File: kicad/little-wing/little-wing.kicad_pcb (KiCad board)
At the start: 4 copper layers, 16.1 x 57.1 mm, 45 parts, among them J1 HRO_TYPE-C-31-M-14, J2 Battery, J3 rgb, J4 columns, J5 Conn_01x10, J6 rows, J7 sensor, SW1 Battery, SW2 Reset, U1 nRF52840_CKAA, U2 nPM1100-CAAx, X1 32MHz, X2 32.768kHz

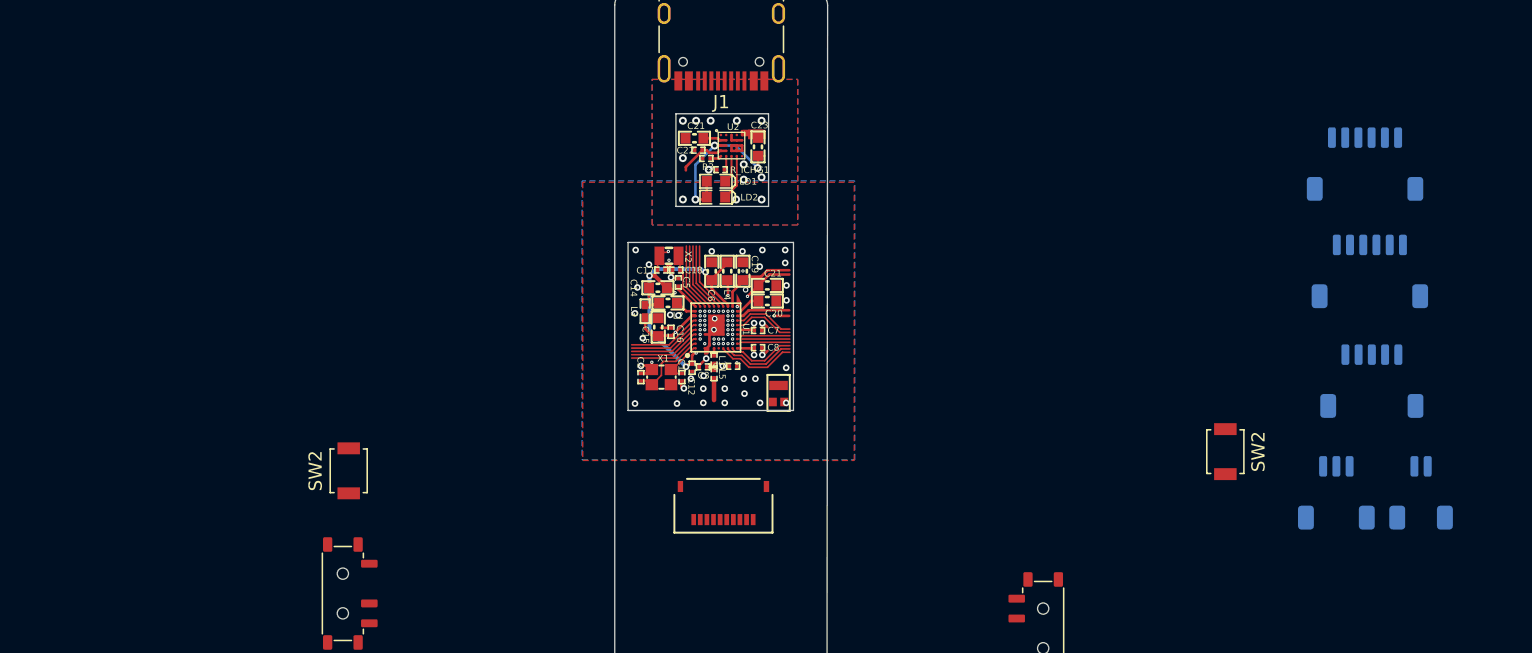
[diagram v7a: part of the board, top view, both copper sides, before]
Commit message: Cleaning up some space on the PCB
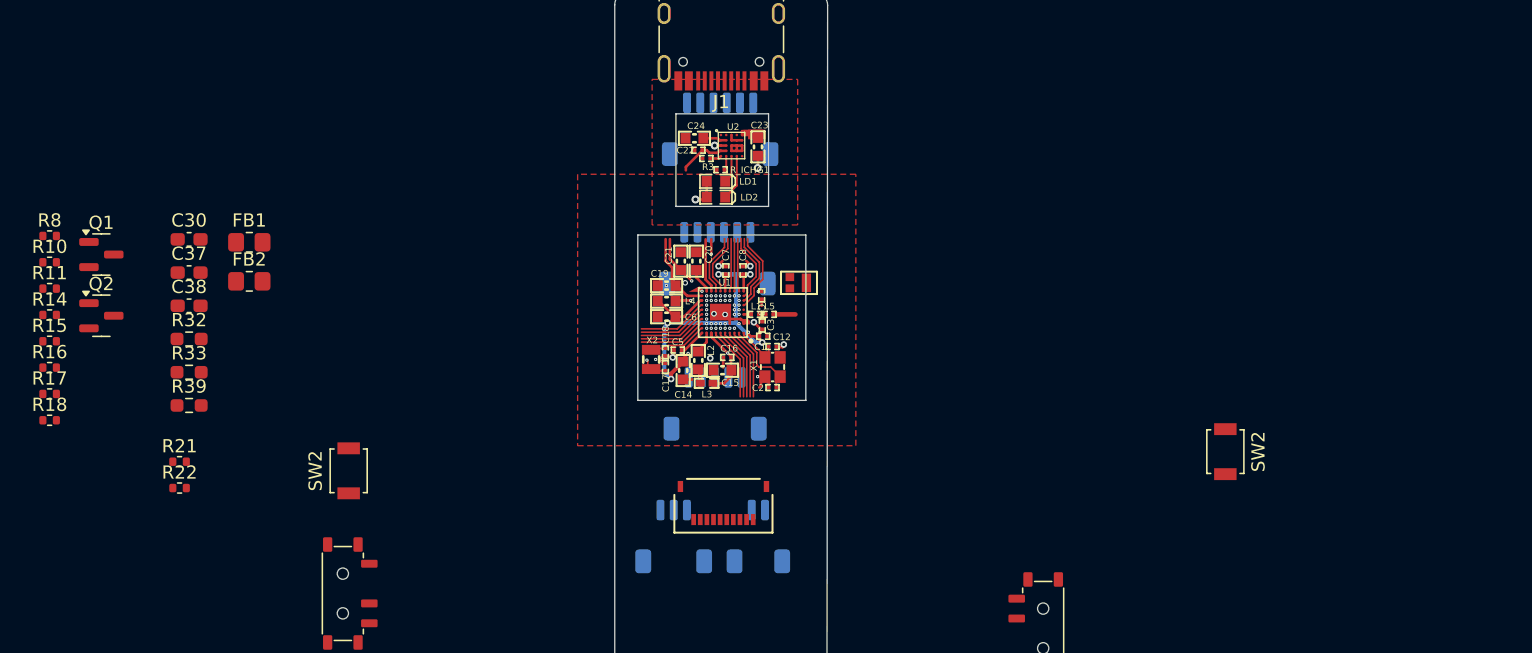
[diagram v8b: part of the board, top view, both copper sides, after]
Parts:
- added C30: 1uF, Capacitor_SMD:C_0603_1608Metric_Pad1.08x0.95mm_HandSolder, F.Cu at (109.8, 76.2)
- added C37: 560pF/680pF, Capacitor_SMD:C_0603_1608Metric_Pad1.08x0.95mm_HandSolder, F.Cu at (109.8, 78.7)
- added C38: 1uF, Capacitor_SMD:C_0603_1608Metric_Pad1.08x0.95mm_HandSolder, F.Cu at (109.8, 81.2)
- added FB1: 2.7k, Resistor_SMD:R_0805_2012Metric_Pad1.20x1.40mm_HandSolder, F.Cu at (114.3, 76.4)
- added FB2: 2.7k, Resistor_SMD:R_0805_2012Metric_Pad1.20x1.40mm_HandSolder, F.Cu at (114.3, 79.3)
- added Q1: AO3401A, Package_TO_SOT_SMD:SOT-23, F.Cu at (103.2, 77.3)
- added Q2: 2N7002, Package_TO_SOT_SMD:SOT-23, F.Cu at (103.2, 82.0)
- added R10: 10k, Resistor_SMD:R_0402_1005Metric, F.Cu at (99.2, 77.9)
- added R11: 100R, Resistor_SMD:R_0402_1005Metric, F.Cu at (99.2, 79.9)
- added R14: 100R, Resistor_SMD:R_0402_1005Metric, F.Cu at (99.2, 81.9)
- added R15: 100R, Resistor_SMD:R_0402_1005Metric, F.Cu at (99.2, 83.9)
- added R16: 100R, Resistor_SMD:R_0402_1005Metric, F.Cu at (99.2, 85.9)
- added R17: 100R, Resistor_SMD:R_0402_1005Metric, F.Cu at (99.2, 87.9)
- added R18: 10k, Resistor_SMD:R_0402_1005Metric, F.Cu at (99.2, 89.8)
- added R21: 5k1, Resistor_SMD:R_0402_1005Metric, F.Cu at (109.1, 93.0)
- added R22: 5k1, Resistor_SMD:R_0402_1005Metric, F.Cu at (109.1, 95.0)
- added R32: 10k, Resistor_SMD:R_0603_1608Metric_Pad0.98x0.95mm_HandSolder, F.Cu at (109.8, 83.7)
- added R33: 10k, Resistor_SMD:R_0603_1608Metric_Pad0.98x0.95mm_HandSolder, F.Cu at (109.8, 86.2)
- added R39: 10k, Resistor_SMD:R_0603_1608Metric_Pad0.98x0.95mm_HandSolder, F.Cu at (109.8, 88.7)
- added R8: 100R, Resistor_SMD:R_0402_1005Metric, F.Cu at (99.2, 75.9)
- moved J7 50.3 mm to (149.9, 67.9)
- moved J3 50.2 mm to (146.4, 98.6)
- moved J2 50.2 mm to (152.8, 98.6)
- moved J6 49.7 mm to (149.5, 88.6)
- moved J4 49.5 mm to (149.7, 77.6)
- moved C2 9.98 mm to (153.9, 87.4), turned to 180 degrees
- moved AE1 8.44 mm to (155.8, 79.5), turned to 0 degrees
- moved X1 8.43 mm to (153.9, 85.8), turned to -90 degrees
- moved X2 7.95 mm to (144.7, 85.3), turned to 90 degrees
- moved C17 7.34 mm to (145.8, 85.8), turned to 90 degrees
- moved C1 7.23 mm to (153.9, 84.3), turned to 0 degrees
- moved L3 7.16 mm to (148.9, 87.1), turned to 180 degrees
- moved C21 6.79 mm to (147.0, 77.8), turned to 90 degrees
- moved C14 6.54 mm to (147.1, 86.1), turned to -90 degrees
- moved C18 6.26 mm to (145.8, 84.7), turned to -90 degrees
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- renumbered C21 to C24
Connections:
- net CHG renamed /Main Module/PSU/CHG
- net DEC1 renamed Net-(U1-DEC1)
- net DEC4_6 renamed Net-(U1-DEC4)
- net ERR renamed /Main Module/PSU/ERR
- net LCD_CLK renamed LCD CLK
- net LCD_CS renamed LCD CS
- net LCD_DATA renamed LCD DATA
- net NetC20_1 renamed Net-(U1-DECUSB)
- net NetC3_2 renamed Net-(C3-Pad2)
- net NetC9_1 renamed Net-(U1-DEC5)
- net NetL1_1 renamed Net-(U1-ANT)
- net NetL2_1 renamed Net-(L2-Pad1)
- net NetL2_2 renamed Net-(U1-DCC)
- net NetL4_2 renamed Net-(U1-DCCH)
- net NetR1_1 renamed Net-(U2-NTC)
- net NetR_ICHG_2 renamed Net-(U2-ICHG)
- net NetU1_A3 renamed Net-(U2-DEC)
- net P0.00/XL1 renamed Net-(U1-P0.00/XL1)
- net P0.01/XL2 renamed Net-(U1-P0.01/XL2)
- net P0.15 renamed BLED
- net P0.31/AIN7 renamed VSENS
- net RF renamed /Main Module/MCU/RF
- net XC1 renamed Net-(U1-XC1)
- net XC2 renamed Net-(U1-XC2)
- AE1 pad 2: GND -> (no net)
- C12 pad 1: VDD_NRF -> VDD
- C14 pad 1: VDD_NRF -> VDD
- C19 pad 1: VDDH -> VSYS
- C23 pad 2: VOUT -> VSYS
- C6 pad 1: VDD_NRF -> VDD
- C7 pad 1: VDD_NRF -> VDD
- C8 pad 1: VDD_NRF -> VDD
- J1 pad A4: +5V -> VBUS
- J1 pad A6: USB-D+ -> D-
- J1 pad A7: USB-D- -> D+
- J1 pad A9: +5V -> VBUS
- J1 pad B4: +5V -> VBUS
- J1 pad B6: USB-D+ -> D-
- J1 pad B7: USB-D- -> D+
- J1 pad B9: +5V -> VBUS
- J3 pad 1: RGB_PWR -> RGB_POWER
- J7 pad 1: +3.3V -> VDD
- L4 pad 1: VDD_NRF -> VDD
- LD1 pad 2: VOUT -> VSYS
- LD2 pad 2: VOUT -> VSYS
- U1 pad A3: P1.11 -> unconnected-(U1-P1.11-PadA3)
- U1 pad A4: P1.13 -> unconnected-(U1-P1.13-PadA4)
- U1 pad A5: P0.03/AIN1 -> unconnected-(U1-P0.03/AIN1-PadA5)
- U1 pad A6: P0.28/AIN4 -> unconnected-(U1-P0.28/AIN4-PadA6)
- U1 pad A7: P0.30/AIN6 -> unconnected-(U1-P0.30/AIN6-PadA7)
- U1 pad B3: VDD_NRF -> VDD
- U1 pad B4: P1.10 -> unconnected-(U1-P1.10-PadB4)
- U1 pad B5: P1.14 -> unconnected-(U1-P1.14-PadB5)
- U1 pad B6: P0.02/AIN0 -> unconnected-(U1-P0.02/AIN0-PadB6)
- U1 pad B8: VDD_NRF -> VDD
- U1 pad C10: P0.04/AIN2 -> unconnected-(U1-P0.04/AIN2-PadC10)
- U1 pad C5: P1.12 -> unconnected-(U1-P1.12-PadC5)
- U1 pad C6: P1.15 -> unconnected-(U1-P1.15-PadC6)
- U1 pad C7: P0.29/AIN5 -> unconnected-(U1-P0.29/AIN5-PadC7)
- U1 pad C9: P0.26 -> unconnected-(U1-P0.26-PadC9)
- U1 pad D10: P0.05/AIN3 -> unconnected-(U1-P0.05/AIN3-PadD10)
- U1 pad D9: P0.27 -> unconnected-(U1-P0.27-PadD9)
- U1 pad E10: P0.08 -> unconnected-(U1-P0.08-PadE10)
- U1 pad E2: P0.10/NFC2 -> unconnected-(U1-P0.10/NFC2-PadE2)
- U1 pad E3: P1.06 -> unconnected-(U1-P1.06-PadE3)
- U1 pad E9: P0.06 -> unconnected-(U1-P0.06-PadE9)
- U1 pad F1: P0.09/NFC1 -> unconnected-(U1-P0.09/NFC1-PadF1)
- U1 pad F10: P1.09 -> unconnected-(U1-P1.09-PadF10)
- U1 pad F3: P1.03 -> unconnected-(U1-P1.03-PadF3)
- U1 pad F9: P0.07 -> unconnected-(U1-P0.07-PadF9)
- U1 pad G1: P1.07 -> unconnected-(U1-P1.07-PadG1)
- U1 pad G10: P0.12 -> unconnected-(U1-P0.12-PadG10)
- U1 pad G2: P1.05 -> unconnected-(U1-P1.05-PadG2)
- U1 pad G3: P1.02 -> unconnected-(U1-P1.02-PadG3)
- U1 pad G9: P1.08 -> unconnected-(U1-P1.08-PadG9)
- U1 pad H1: P1.04 -> unconnected-(U1-P1.04-PadH1)
- U1 pad H10: VDD_NRF -> VDD
- U1 pad H2: SWDCLK -> unconnected-(U1-SWDCLK-PadH2)
- U1 pad H4: P0.24 -> unconnected-(U1-P0.24-PadH4)
- U1 pad H5: P0.23 -> unconnected-(U1-P0.23-PadH5)
- U1 pad H6: P0.16 -> unconnected-(U1-P0.16-PadH6)
- U1 pad H7: P0.13 -> unconnected-(U1-P0.13-PadH7)
- U1 pad H8: P0.11 -> unconnected-(U1-P0.11-PadH8)
- U1 pad J1: P1.01 -> unconnected-(U1-P1.01-PadJ1)
- U1 pad J10: VDDH -> VSYS
- U1 pad J2: SWDIO -> unconnected-(U1-SWDIO-PadJ2)
- U1 pad J3: P1.00 -> unconnected-(U1-P1.00-PadJ3)
- U1 pad J4: P0.21 -> unconnected-(U1-P0.21-PadJ4)
- U1 pad J5: P0.20 -> unconnected-(U1-P0.20-PadJ5)
- U1 pad J6: P0.17 -> unconnected-(U1-P0.17-PadJ6)
- U1 pad J7: P0.14 -> unconnected-(U1-P0.14-PadJ7)
- U1 pad K1: VDD_NRF -> VDD
- U1 pad K2: P0.25 -> unconnected-(U1-P0.25-PadK2)
- U1 pad K3: P0.22 -> unconnected-(U1-P0.22-PadK3)
- U1 pad K4: P0.19 -> unconnected-(U1-P0.19-PadK4)
- U1 pad K5: VDD_NRF -> VDD
- U1 pad K6: P0.18/RESET -> RST
- U2 pad A1: GND -> D+
- U2 pad A2: (no net) -> D-
- U2 pad A4: (no net) -> unconnected-(U2-SW-PadA4)
- U2 pad C1: VOUT -> VSYS
- U2 pad C2: VOUT -> VSYS
- X1 pad 2: GND -> unconnected-(X1-GND-Pad2)
- X1 pad 4: GND -> unconnected-(X1-GND-Pad4)
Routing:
- net VDD_NRF: track 37.7 -> 0.00 mm, vias 9 -> 0
- net VDD: track 0.00 -> 37.2 mm, vias 0 -> 9
- net VSYS: track 0.00 -> 19.3 mm, vias 0 -> 3
- net P1.03: track 13.4 -> 0.00 mm, vias 2 -> 0
- net unconnected-(U1-P1.03-PadF3): track 0.00 -> 13.4 mm, vias 0 -> 2
- net VOUT: track 13.1 -> 0.00 mm, vias 3 -> 0
- net unconnected-(U1-P1.06-PadE3): track 0.00 -> 12.6 mm, vias 0 -> 2
- net P1.06: track 12.6 -> 0.00 mm, vias 2 -> 0
- net unconnected-(U1-P1.02-PadG3): track 0.00 -> 11.0 mm, vias 0 -> 2
- net P1.02: track 11.0 -> 0.00 mm, vias 2 -> 0
- net unconnected-(U1-P0.24-PadH4): track 0.00 -> 9.56 mm, vias 0 -> 2
- net P0.24: track 9.56 -> 0.00 mm, vias 2 -> 0
- net unconnected-(U1-P0.23-PadH5): track 0.00 -> 9.47 mm, vias 0 -> 2
- net P0.23: track 9.47 -> 0.00 mm, vias 2 -> 0
- net unconnected-(U1-P0.16-PadH6): track 0.00 -> 8.49 mm, vias 0 -> 2
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- removed copper zone on B.Cu, net GND
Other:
- outline, holes or cut-outs redrawn
